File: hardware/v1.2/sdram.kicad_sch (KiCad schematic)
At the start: 8 parts, among them U1 ECP5-CABGA256, U10 W9825G6KH

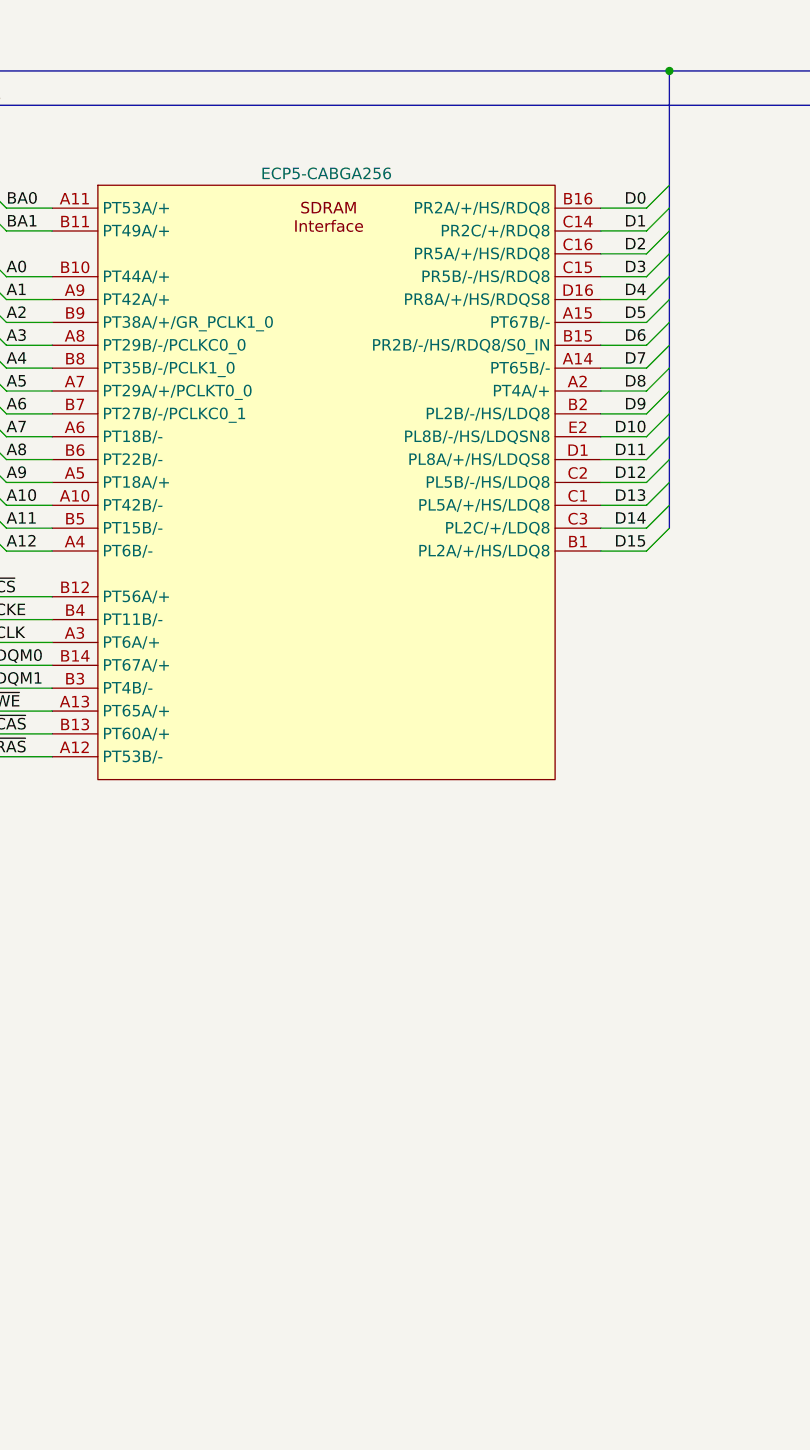
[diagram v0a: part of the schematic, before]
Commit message: UART to PS2 converter
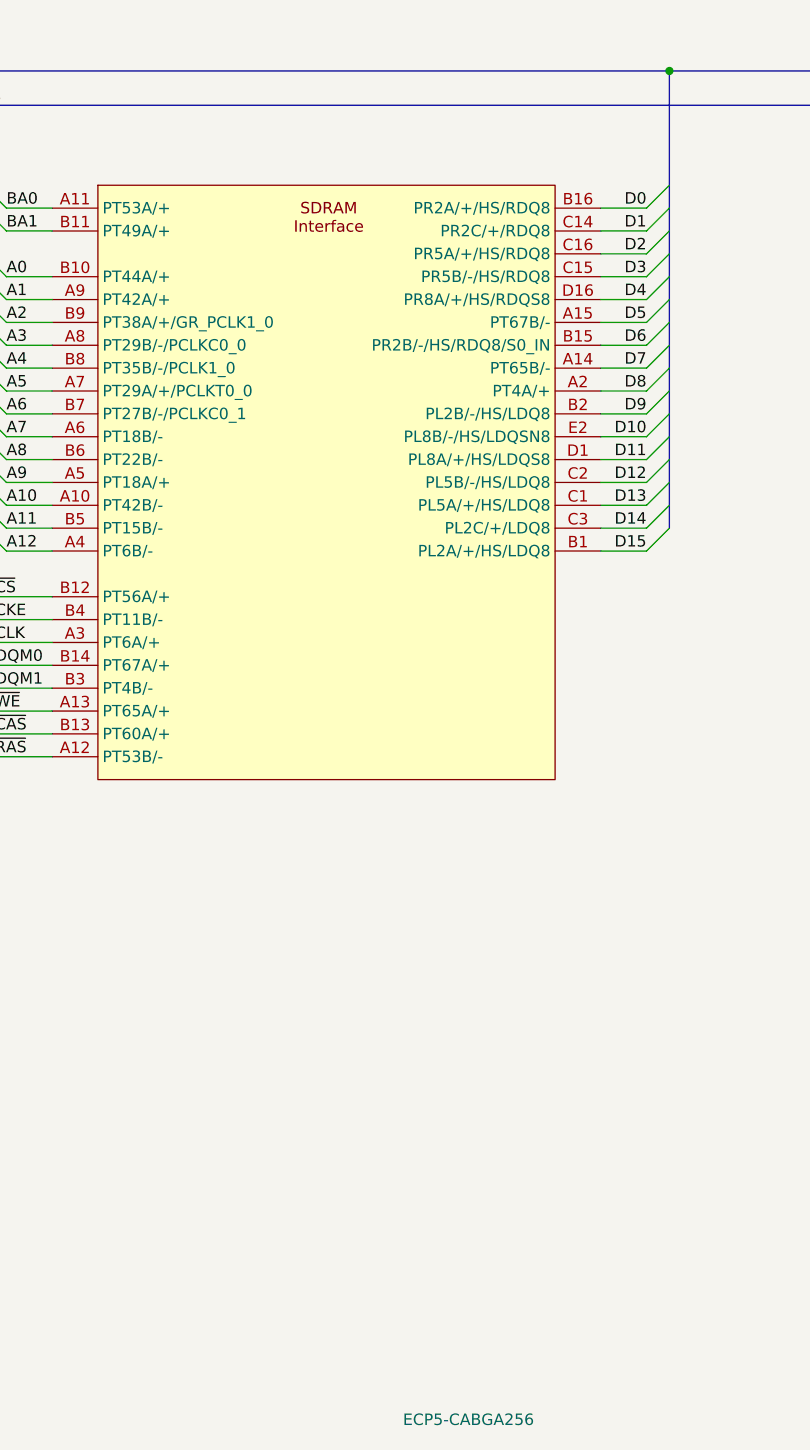
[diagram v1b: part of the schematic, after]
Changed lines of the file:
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@@
 		)
 		(property "Value" "ECP5-CABGA256"
-			(at 91.44 66.04 0)
+			(at 99.9333 204.47 0)
 			(effects
 				(font
 					(size 1.27 1.27)
 				)
+				(justify left)
 			)
 		)
@@
 		)
 		(instances
-			(project "icepi-zero"
+			(project ""
+				(path "/f88da08e-cf42-4d03-a08f-3f602fe6658d/17c9c9b3-f379-4e1f-a876-d3fcf0529a4d"
+					(reference "U1")
+					(unit 6)
+				)
 				(path "/f88da08e-cf42-4d03-a08f-3f602fe6658d/3bffbb9a-e009-498c-a1b0-c490cdf30139"
 					(reference "U1")
